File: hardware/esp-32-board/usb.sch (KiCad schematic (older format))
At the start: 8 parts, among them J5 USB_B_Micro, Q1 BCR129S, U2 USBLC6-2SC6, U3 CP2102N-A01-GQFN28

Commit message: Update USB connector
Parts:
- added C10: 22uF, Capacitor_SMD:C_0805_2012Metric_Pad1.18x1.45mm_HandSolder, symbol Device:C
- J5: footprint Connector_USB:USB_Micro-B_Molex_47346-0001 -> Connector_USB:USB_Micro-B_Molex-105017-0001; symbol Connector:USB_A -> Connector:USB_B_Micro; Vendor (none) -> tme.eu; VendorLink (none) -> https://www.tme.eu/pl/details/mx-105017-0001/zlacza-usb-i-i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
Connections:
- wire segments 60 -> 64
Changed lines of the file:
@@
 	5500 3450 5500 3650
 $Comp
-L Connector:USB_A J?
+L Connector:USB_B_Micro J?
 U 1 1 5FFC9948
 P 1550 2400
@@
 F 0 "J5" H 1650 2900 50  0000 C CNN
 F 1 "USB_B_Micro" H 1650 2800 50  0000 C CNN
-F 2 "Connector_USB:USB_Micro-B_Molex_47346-0001" H 1700 2350 50  0001 C CNN
-F 3 " ~" H 1700 2350 50  0001 C CNN
+F 2 "Connector_USB:USB_Micro-B_Molex-105017-0001" H 1700 2350 50  0001 C CNN
+F 3 "https://www.tme.eu/Document/b7989e722b05f5084c507fb3ad8f02cb/MX-105017-0001.pdf" H 1700 2350 50  0001 C CNN
+F 4 "tme.eu" H 1550 2400 50  0001 C CNN "Vendor"
+F 5 "https://www.tme.eu/pl/details/mx-105017-0001/zlacza-usb-i-ieee1394/molex/105017-0001/" H 1550 2400 50  0001 C CNN "VendorLink"
 	1    1550 2400
 	1    0    0    -1
 $EndComp
-Wire Wire Line
-	1450 2800 1450 3600
 Wire Wire Line
 	1450 3600 1550 3600
@@
 	1550 3600 1800 3600
 Connection ~ 1550 3600
-Wire Wire Line
-	1800 3600 2450 3600
 Wire Wire Line
 	2450 3600 2450 3350
@@
 Wire Wire Line
 	1950 2850 2050 2850
+Wire Wire Line
+	1850 2600 1900 2600
+Wire Wire Line
+	1900 2600 1900 3600
+Wire Wire Line
+	1800 3600 1900 3600
+Connection ~ 1900 3600
+Wire Wire Line
+	1900 3600 2450 3600
+$Comp
+L Device:C C?
+U 1 1 5FBBB3E1
+P 1450 3100
+AR Path="/5FBBB3E1" Ref="C?"  Part="1"
+AR Path="/5FF6344B/5FBBB3E1" Ref="C?"  Part="1"
+AR Path="/5FF73D59/5FBBB3E1" Ref="C10"  Part="1"
+F 0 "C10" H 1500 3200 50  0000 L CNN
+F 1 "22uF" H 1500 3000 50  0000 L CNN
+F 2 "Capacitor_SMD:C_0805_2012Metric_Pad1.18x1.45mm_HandSolder" H 1488 2950 50  0001 C CNN
+F 3 "~" H 1450 3100 50  0001 C CNN
+F 4 "tme.eu" H 1450 3100 50  0001 C CNN "Vendor"
+F 5 "https://www.tme.eu/pl/details/cl21a226mqqnnng/kondensatory-mlcc-smd-0805/samsung/" H 1450 3100 50  0001 C CNN "VendorLink"
+	1    1450 3100
+	1    0    0    -1
+$EndComp
+Wire Wire Line
+	1450 2800 1450 2950
+Wire Wire Line
+	1450 3250 1450 3600
 $EndSCHEMATC

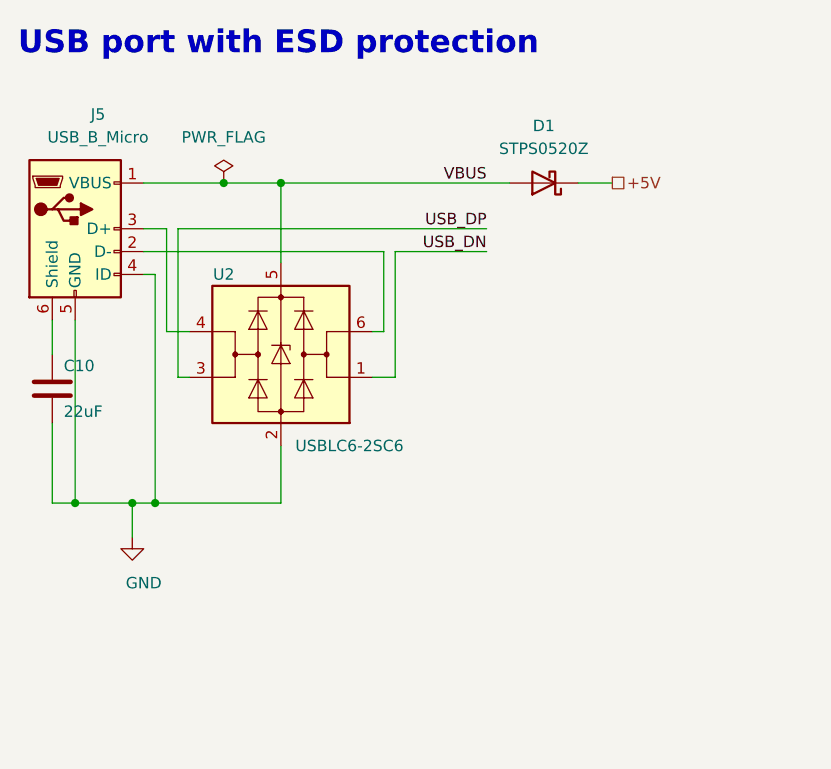
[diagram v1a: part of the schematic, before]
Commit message: Change microUSB
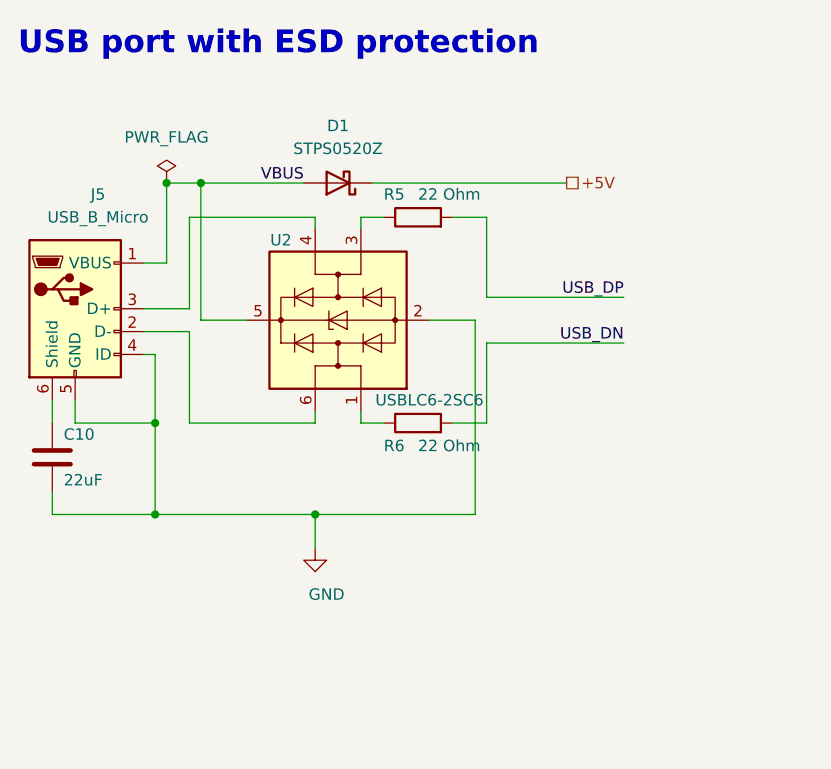
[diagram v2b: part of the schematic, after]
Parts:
- added R5, R6: 22 Ohm, Resistor_SMD:R_0805_2012Metric_Pad1.20x1.40mm_HandSolder, symbol Device:R
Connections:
- net USB_DN: now also R6.2; no longer U2.1 (I/O1)
- net USB_DP: now also R5.2; no longer U2.3 (I/O2)
- new net: R5.1, U2.3 (I/O2)
- new net: R6.1, U2.1 (I/O1)
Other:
- moved on the sheet: C10, D1, J5, U2
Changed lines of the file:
@@
 L Connector:USB_B_Micro J?
 U 1 1 5FFC9948
-P 1550 2400
+P 1550 2750
 AR Path="/5FFC9948" Ref="J?"  Part="1"
 AR Path="/5FF73D59/5FFC9948" Ref="J5"  Part="1"
-F 0 "J5" H 1650 2900 50  0000 C CNN
-F 1 "USB_B_Micro" H 1650 2800 50  0000 C CNN
-F 2 "Connector_USB:USB_Micro-B_Molex-105017-0001" H 1700 2350 50  0001 C CNN
-F 3 "https://www.tme.eu/Document/b7989e722b05f5084c507fb3ad8f02cb/MX-105017-0001.pdf" H 1700 2350 50  0001 C CNN
-F 4 "tme.eu" H 1550 2400 50  0001 C CNN "Vendor"
-F 5 "https://www.tme.eu/pl/details/mx-105017-0001/zlacza-usb-i-ieee1394/molex/105017-0001/" H 1550 2400 50  0001 C CNN "VendorLink"
-	1    1550 2400
-	1    0    0    -1
-$EndComp
-Wire Wire Line
-	1450 3600 1550 3600
-Wire Wire Line
-	1550 2800 1550 3600
-Text Label 3350 2500 2    50   ~ 0
+F 0 "J5" H 1650 3250 50  0000 C CNN
+F 1 "USB_B_Micro" H 1650 3150 50  0000 C CNN
+F 2 "Connector_USB:USB_Micro-B_Molex-105017-0001" H 1700 2700 50  0001 C CNN
+F 3 "https://www.tme.eu/Document/b7989e722b05f5084c507fb3ad8f02cb/MX-105017-0001.pdf" H 1700 2700 50  0001 C CNN
+F 4 "tme.eu" H 1550 2750 50  0001 C CNN "Vendor"
+F 5 "https://www.tme.eu/pl/details/mx-105017-0001/zlacza-usb-i-ieee1394/molex/105017-0001/" H 1550 2750 50  0001 C CNN "VendorLink"
+	1    1550 2750
+	1    0    0    -1
+$EndComp
+Text Label 3950 2900 2    50   ~ 0
 USB_DN
 Text Label 8800 2100 0    50   ~ 0
@@
 L power:GND #PWR?
 U 1 1 5FFC9960
-P 1800 3750
+P 2600 3800
 AR Path="/5FFC9960" Ref="#PWR?"  Part="1"
 AR Path="/5FF73D59/5FFC9960" Ref="#PWR023"  Part="1"
-F 0 "#PWR023" H 1800 3500 50  0001 C CNN
-F 1 "GND" H 1850 3550 50  0000 C CNN
-F 2 "" H 1800 3750 50  0001 C CNN
-F 3 "" H 1800 3750 50  0001 C CNN
-	1    1800 3750
-	1    0    0    -1
-$EndComp
-Wire Wire Line
-	1800 3750 1800 3600
+F 0 "#PWR023" H 2600 3550 50  0001 C CNN
+F 1 "GND" H 2650 3600 50  0000 C CNN
+F 2 "" H 2600 3800 50  0001 C CNN
+F 3 "" H 2600 3800 50  0001 C CNN
+	1    2600 3800
+	1    0    0    -1
+$EndComp
+Wire Wire Line
+	2600 3800 2600 3650
 Wire Wire Line
 	5500 2200 5250 2200
@@
 Wire Wire Line
 	6700 5000 6700 5350
-Text Label 3350 2400 2    50   ~ 0
+Text Label 3950 2700 2    50   ~ 0
 USB_DP
-Wire Wire Line
-	1850 2500 2900 2500
-Wire Wire Line
-	2450 2550 2450 2200
-Wire Wire Line
-	1550 3600 1800 3600
-Connection ~ 1550 3600
-Wire Wire Line
-	2450 3600 2450 3350
-Connection ~ 1800 3600
-$Comp
-L Power_Protection:USBLC6-2SC6 U2
-U 1 1 601988F8
-P 2450 2950
-F 0 "U2" H 2700 3300 50  0000 C CNN
-F 1 "USBLC6-2SC6" H 2150 2550 50  0000 C CNN
-F 2 "Package_TO_SOT_SMD:SOT-23-6" H 2450 2450 50  0001 C CNN
-F 3 "https://www.st.com/resource/en/datasheet/usblc6-2.pdf" H 2650 3300 50  0001 C CNN
-F 4 "tme.eu" H 2450 2950 50  0001 C CNN "Vendor"
-F 5 "https://www.tme.eu/pl/details/usblc6-2sc6/diody-zabezpieczajace-drabinki/stmicroelectronics/" H 2450 2950 50  0001 C CNN "VendorLink"
-	1    2450 2950
-	-1   0    0    -1
-$EndComp
-Wire Wire Line
-	1850 2400 1950 2400
-Wire Wire Line
-	2000 2400 3350 2400
 Text HLabel 5500 1850 0    50   UnSpc ~ 0
 Internal_3V3
@@
 L Device:D_Schottky D?
 U 1 1 5FB2216A
-P 3600 2200
+P 2700 2200
 AR Path="/5FB2216A" Ref="D?"  Part="1"
 AR Path="/5FF6344B/5FB2216A" Ref="D?"  Part="1"
 AR Path="/5FF73D59/5FB2216A" Ref="D1"  Part="1"
-F 0 "D1" H 3600 1950 50  0000 C CNN
-F 1 "STPS0520Z" H 3600 2050 50  0000 C CNN
-F 2 "Diode_SMD:D_SOD-123" H 3600 2200 50  0001 C CNN
-F 3 "https://www.st.com/resource/en/datasheet/stps0520z.pdf" H 3600 2200 50  0001 C CNN
-F 4 "tme.eu" H 3600 2200 50  0001 C CNN "Vendor"
-F 5 "https://www.tme.eu/pl/details/stps0520z/diody-schottky-smd/stmicroelectronics/" H 3600 2200 50  0001 C CNN "VendorLink"
-	1    3600 2200
+F 0 "D1" H 2700 1950 50  0000 C CNN
+F 1 "STPS0520Z" H 2700 2050 50  0000 C CNN
+F 2 "Diode_SMD:D_SOD-123" H 2700 2200 50  0001 C CNN
+F 3 "https://www.st.com/resource/en/datasheet/stps0520z.pdf" H 2700 2200 50  0001 C CNN
+F 4 "tme.eu" H 2700 2200 50  0001 C CNN "Vendor"
+F 5 "https://www.tme.eu/pl/details/stps0520z/diody-schottky-smd/stmicroelectronics/" H 2700 2200 50  0001 C CNN "VendorLink"
+	1    2700 2200
 	-1   0    0    1
 $EndComp
-Wire Wire Line
-	3750 2200 3900 2200
-Text HLabel 3900 2200 2    50   UnSpc ~ 0
+Text HLabel 3700 2200 2    50   UnSpc ~ 0
 +5V
-Text Label 3350 2200 2    50   ~ 0
+Text Label 2550 2200 2    50   ~ 0
 VBUS
 $Comp
@@
 	1    0    0    -1
 $EndComp
-Connection ~ 2450 2200
 Text Notes 1300 1650 0    100  ~ 20
 USB port with ESD protection
@@
 NoConn ~ 7200 3500
 Wire Wire Line
-	2200 2200 2450 2200
-Wire Wire Line
-	1850 2200 2200 2200
-Connection ~ 2200 2200
+	1850 2550 1950 2550
 $Comp
 L power:PWR_FLAG #FLG0104
 U 1 1 5FCE0047
-P 2200 2200
-F 0 "#FLG0104" H 2200 2275 50  0001 C CNN
-F 1 "PWR_FLAG" H 2200 2400 50  0000 C CNN
-F 2 "" H 2200 2200 50  0001 C CNN
-F 3 "~" H 2200 2200 50  0001 C CNN
-	1    2200 2200
-	1    0    0    -1
-$EndComp
-Wire Wire Line
-	2450 2200 3450 2200
-Wire Wire Line
-	2950 2500 3350 2500
-Wire Wire Line
-	2950 3050 2850 3050
-Wire Wire Line
-	2900 2500 2900 2850
-Wire Wire Line
-	2900 2850 2850 2850
-Wire Wire Line
-	2950 2500 2950 3050
-Wire Wire Line
-	2000 2400 2000 3050
-Wire Wire Line
-	2000 3050 2050 3050
-Wire Wire Line
-	1950 2400 1950 2850
-Wire Wire Line
-	1950 2850 2050 2850
-Wire Wire Line
-	1850 2600 1900 2600
-Wire Wire Line
-	1900 2600 1900 3600
-Wire Wire Line
-	1800 3600 1900 3600
-Connection ~ 1900 3600
-Wire Wire Line
-	1900 3600 2450 3600
+P 1950 2200
+F 0 "#FLG0104" H 1950 2275 50  0001 C CNN
+F 1 "PWR_FLAG" H 1950 2400 50  0000 C CNN
+F 2 "" H 1950 2200 50  0001 C CNN
+F 3 "~" H 1950 2200 50  0001 C CNN
+	1    1950 2200
+	1    0    0    -1
+$EndComp
+Wire Wire Line
+	1850 2950 1900 2950
+Wire Wire Line
+	1900 2950 1900 3250
 $Comp
 L Device:C C?
 U 1 1 5FBBB3E1
-P 1450 3100
+P 1450 3400
 AR Path="/5FBBB3E1" Ref="C?"  Part="1"
 AR Path="/5FF6344B/5FBBB3E1" Ref="C?"  Part="1"
 AR Path="/5FF73D59/5FBBB3E1" Ref="C10"  Part="1"
-F 0 "C10" H 1500 3200 50  0000 L CNN
-F 1 "22uF" H 1500 3000 50  0000 L CNN
-F 2 "Capacitor_SMD:C_0805_2012Metric_Pad1.18x1.45mm_HandSolder" H 1488 2950 50  0001 C CNN
-F 3 "~" H 1450 3100 50  0001 C CNN
-F 4 "tme.eu" H 1450 3100 50  0001 C CNN "Vendor"
-F 5 "https://www.tme.eu/pl/details/cl21a226mqqnnng/kondensatory-mlcc-smd-0805/samsung/" H 1450 3100 50  0001 C CNN "VendorLink"
-	1    1450 3100
-	1    0    0    -1
-$EndComp
-Wire Wire Line
-	1450 2800 1450 2950
-Wire Wire Line
-	1450 3250 1450 3600
+F 0 "C10" H 1500 3500 50  0000 L CNN
+F 1 "22uF" H 1500 3300 50  0000 L CNN
+F 2 "Capacitor_SMD:C_0805_2012Metric_Pad1.18x1.45mm_HandSolder" H 1488 3250 50  0001 C CNN
+F 3 "~" H 1450 3400 50  0001 C CNN
+F 4 "tme.eu" H 1450 3400 50  0001 C CNN "Vendor"
+F 5 "https://www.tme.eu/pl/details/cl21a226mqqnnng/kondensatory-mlcc-smd-0805/samsung/" H 1450 3400 50  0001 C CNN "VendorLink"
+	1    1450 3400
+	1    0    0    -1
+$EndComp
+Wire Wire Line
+	1450 3150 1450 3250
+Wire Wire Line
+	1450 3550 1450 3650
+$Comp
+L Power_Protection:USBLC6-2SC6 U2
+U 1 1 601988F8
+P 2700 2800
+F 0 "U2" V 3050 3050 50  0000 C CNN
+F 1 "USBLC6-2SC6" V 2350 2400 50  0000 C CNN
+F 2 "Package_TO_SOT_SMD:SOT-23-6" H 2700 2300 50  0001 C CNN
+F 3 "https://www.st.com/resource/en/datasheet/usblc6-2.pdf" H 2900 3150 50  0001 C CNN
+F 4 "tme.eu" H 2700 2800 50  0001 C CNN "Vendor"
+F 5 "https://www.tme.eu/pl/details/usblc6-2sc6/diody-zabezpieczajace-drabinki/stmicroelectronics/" H 2700 2800 50  0001 C CNN "VendorLink"
+	1    2700 2800
+	0    -1   -1   0
+$EndComp
+Wire Wire Line
+	1950 2200 1950 2550
+Connection ~ 1950 2200
+Wire Wire Line
+	1850 2750 2050 2750
+Wire Wire Line
+	2050 2750 2050 2350
+Wire Wire Line
+	2600 2350 2600 2400
+Wire Wire Line
+	2800 2400 2800 2350
+Wire Wire Line
+	3350 2350 3350 2700
+Wire Wire Line
+	3350 2700 3950 2700
+Wire Wire Line
+	1850 2850 2050 2850
+Wire Wire Line
+	2050 2850 2050 3250
+Wire Wire Line
+	2600 3250 2600 3200
+Wire Wire Line
+	2800 3200 2800 3250
+Wire Wire Line
+	3350 3250 3350 2900
+Wire Wire Line
+	3350 2900 3950 2900
+Wire Wire Line
+	3300 3650 2600 3650
+Connection ~ 1900 3650
+Wire Wire Line
+	3100 2800 3300 2800
+Wire Wire Line
+	1950 2200 2100 2200
+Wire Wire Line
+	3300 2800 3300 3650
+Wire Wire Line
+	2300 2800 2100 2800
+Wire Wire Line
+	2100 2800 2100 2200
+Connection ~ 2100 2200
+Wire Wire Line
+	2100 2200 2550 2200
+Connection ~ 2600 3650
+Wire Wire Line
+	1900 3650 2600 3650
+Wire Wire Line
+	1450 3650 1900 3650
+Wire Wire Line
+	1550 3150 1550 3250
+Wire Wire Line
+	1550 3250 1900 3250
+Connection ~ 1900 3250
+Wire Wire Line
+	1900 3250 1900 3650
+Wire Wire Line
+	2850 2200 3700 2200
+$Comp
+L Device:R R?
+U 1 1 5FC3959C
+P 3050 2350
+AR Path="/5FC3959C" Ref="R?"  Part="1"
+AR Path="/5FF73D59/5FC3959C" Ref="R5"  Part="1"
+F 0 "R5" V 3150 2500 50  0000 R CNN
+F 1 "22 Ohm" V 3150 2350 50  0000 R CNN
+F 2 "Resistor_SMD:R_0805_2012Metric_Pad1.20x1.40mm_HandSolder" V 2980 2350 50  0001 C CNN
+F 3 "~" H 3050 2350 50  0001 C CNN
+F 4 "avt.pl" H 3050 2350 50  0001 C CNN "Vendor"
+F 5 "https://sklep.avt.pl/avt701-805.html" H 3050 2350 50  0001 C CNN "VendorLink"
+	1    3050 2350
+	0    -1   -1   0
+$EndComp
+$Comp
+L Device:R R?
+U 1 1 5FC43B6A
+P 3050 3250
+AR Path="/5FC43B6A" Ref="R?"  Part="1"
+AR Path="/5FF73D59/5FC43B6A" Ref="R6"  Part="1"
+F 0 "R6" V 2950 3400 50  0000 R CNN
+F 1 "22 Ohm" V 2950 3250 50  0000 R CNN
+F 2 "Resistor_SMD:R_0805_2012Metric_Pad1.20x1.40mm_HandSolder" V 2980 3250 50  0001 C CNN
+F 3 "~" H 3050 3250 50  0001 C CNN
+F 4 "avt.pl" H 3050 3250 50  0001 C CNN "Vendor"
+F 5 "https://sklep.avt.pl/avt701-805.html" H 3050 3250 50  0001 C CNN "VendorLink"
+	1    3050 3250
+	0    -1   -1   0
+$EndComp
+Wire Wire Line
+	2050 2350 2600 2350
+Wire Wire Line
+	2050 3250 2600 3250
+Wire Wire Line
+	2800 2350 2900 2350
+Wire Wire Line
+	3200 2350 3350 2350
+Wire Wire Line
+	3200 3250 3350 3250
+Wire Wire Line
+	2800 3250 2900 3250
 $EndSCHEMATC

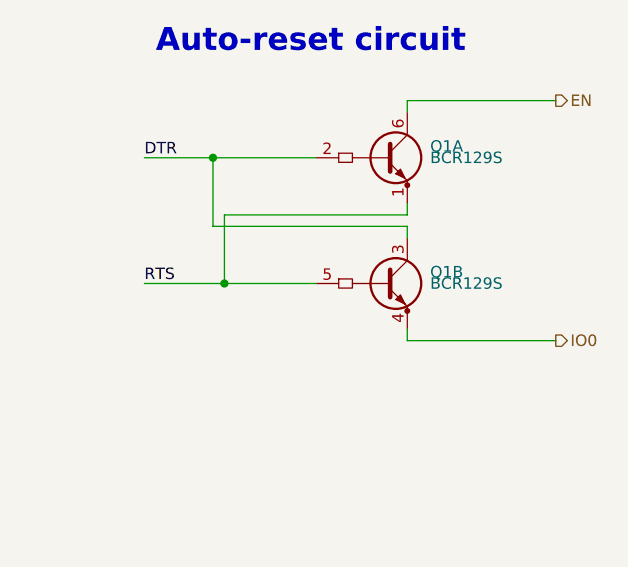
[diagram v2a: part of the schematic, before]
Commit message: Fix auto-reset circuit connections
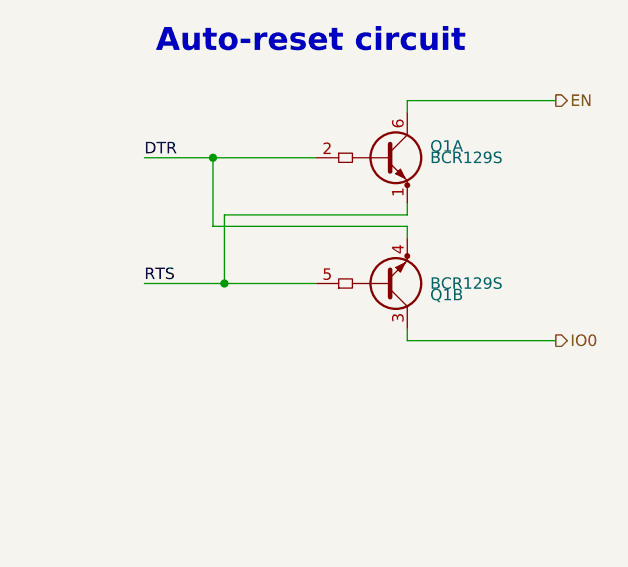
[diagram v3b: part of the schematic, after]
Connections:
- net DTR: now also Q1.4 (E2); no longer Q1.3 (C1)
- net IO0: now also Q1.3 (C1); no longer Q1.4 (E2)
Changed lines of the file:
@@
 F 5 "https://www.tme.eu/pl/details/bcr129sh6327/tranzystory-npn-smd/infineon-technologies/" H 9900 2650 50  0001 C CNN "VendorLink"
 	2    9900 2650
-	1    0    0    -1
+	1    0    0    1
 $EndComp
 Text Notes 1300 1650 0    100  ~ 20
